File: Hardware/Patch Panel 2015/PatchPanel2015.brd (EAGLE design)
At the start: 226 x 119 mm, 35 parts

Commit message: Hi
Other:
- board size 226 x 119 mm -> 209.6 x 127 mm
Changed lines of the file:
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@@
 <?xml version="1.0" encoding="utf-8"?>
 <!DOCTYPE eagle SYSTEM "eagle.dtd">
-<eagle version="7.0.0">
+<eagle version="7.2.0">
 <drawing>
 <settings>
@@
 <board>
 <plain>
-<wire x1="0" y1="0" x2="226.04" y2="0" width="0" layer="20"/>
-<wire x1="226.04" y1="0" x2="226.04" y2="119.05" width="0" layer="20"/>
-<wire x1="226.04" y1="119.05" x2="0" y2="119.05" width="0" layer="20"/>
-<wire x1="0" y1="119.05" x2="0" y2="0" width="0" layer="20"/>
+<wire x1="0" y1="0" x2="209.55" y2="0" width="0" layer="20"/>
+<wire x1="209.55" y1="0" x2="209.55" y2="127" width="0" layer="20"/>
+<wire x1="209.55" y1="127" x2="0" y2="127" width="0" layer="20"/>
+<wire x1="0" y1="127" x2="0" y2="0" width="0" layer="20"/>
 <hole x="6.35" y="6.35" drill="5.5372"/>
 <hole x="50.8" y="6.35" drill="5.5372"/>

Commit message: hi eric, how are you?
also I made slight changes on the patch panel.
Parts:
- added EXT_MOTOR_1, EXT_MOTOR_2, EXT_MOTOR_3, EXT_MOTOR_4, EXT_MOTOR_5, EXT_MOTOR_6: XT60_BOARD_MOUNT, MRDT-2015-PowerBoard:XT60_BOARD
- added INT_MOTOR_1, INT_MOTOR_2, INT_MOTOR_3, INT_MOTOR_4, INT_MOTOR_5, INT_MOTOR_6: H_20020618-M02VERT, MRDT-2015-PowerBoard:20020620-M02
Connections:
- removed net VEE: ETH_IN7.4, ETH_IN7.5, ETH_OUT7.4, ETH_OUT7.5
- new net N$12: EXT_MOTOR_3.POS, INT_MOTOR_3.L1, INT_MOTOR_3.L2
- new net N$13: EXT_MOTOR_3.NEG, INT_MOTOR_3.R1, INT_MOTOR_3.R2
- new net N$15: EXT_MOTOR_4.POS, INT_MOTOR_4.L1, INT_MOTOR_4.L2
- new net N$16: EXT_MOTOR_4.NEG, INT_MOTOR_4.R1, INT_MOTOR_4.R2
- new net N$20: EXT_MOTOR_5.POS, INT_MOTOR_5.L1, INT_MOTOR_5.L2
- new net N$21: EXT_MOTOR_5.NEG, INT_MOTOR_5.R1, INT_MOTOR_5.R2
- new net N$23: EXT_MOTOR_6.POS, INT_MOTOR_6.L1, INT_MOTOR_6.L2
- new net N$24: EXT_MOTOR_6.NEG, INT_MOTOR_6.R1, INT_MOTOR_6.R2
- new net N$4: EXT_MOTOR_1.POS, INT_MOTOR_1.L1, INT_MOTOR_1.L2
- new net N$5: EXT_MOTOR_1.NEG, INT_MOTOR_1.R1, INT_MOTOR_1.R2
- new net N$7: EXT_MOTOR_2.POS, INT_MOTOR_2.L1, INT_MOTOR_2.L2
- new net N$8: EXT_MOTOR_2.NEG, INT_MOTOR_2.R1, INT_MOTOR_2.R2
- net +12V: now also ETH_IN7.4, ETH_IN7.5, ETH_OUT7.4, ETH_OUT7.5
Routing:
- net N$42: track 37.1 -> 0.00 mm
- net N$18: track 37.1 -> 0.00 mm
- net N$2: track 37.1 -> 0.00 mm
- net N$10: track 37.1 -> 0.00 mm
- net N$39: track 37.1 -> 0.00 mm
- net N$31: track 37.1 -> 0.00 mm
- net N$9: track 28.4 -> 0.00 mm
- net N$1: track 28.4 -> 0.00 mm
- net N$41: track 28.4 -> 0.00 mm
- net N$32: track 28.4 -> 0.00 mm
- net N$17: track 28.4 -> 0.00 mm
- net N$40: track 28.4 -> 0.00 mm
- net N$6: track 27.1 -> 0.00 mm
- net N$46: track 27.1 -> 0.00 mm
- net N$35: track 27.1 -> 0.00 mm
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
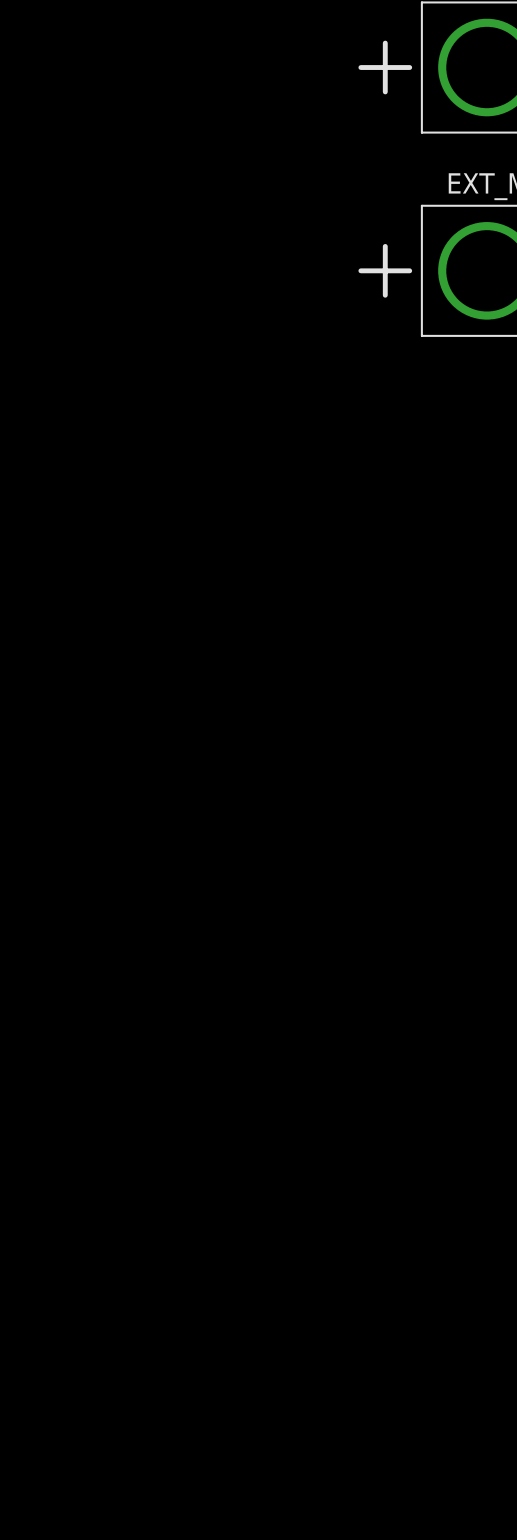
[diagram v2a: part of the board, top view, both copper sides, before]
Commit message: Eric, pls respond
Also, patch panel schematic is usable, but I haven’t started placement
or routing yet. I want to add PTCs to all of the PoRC outputs.
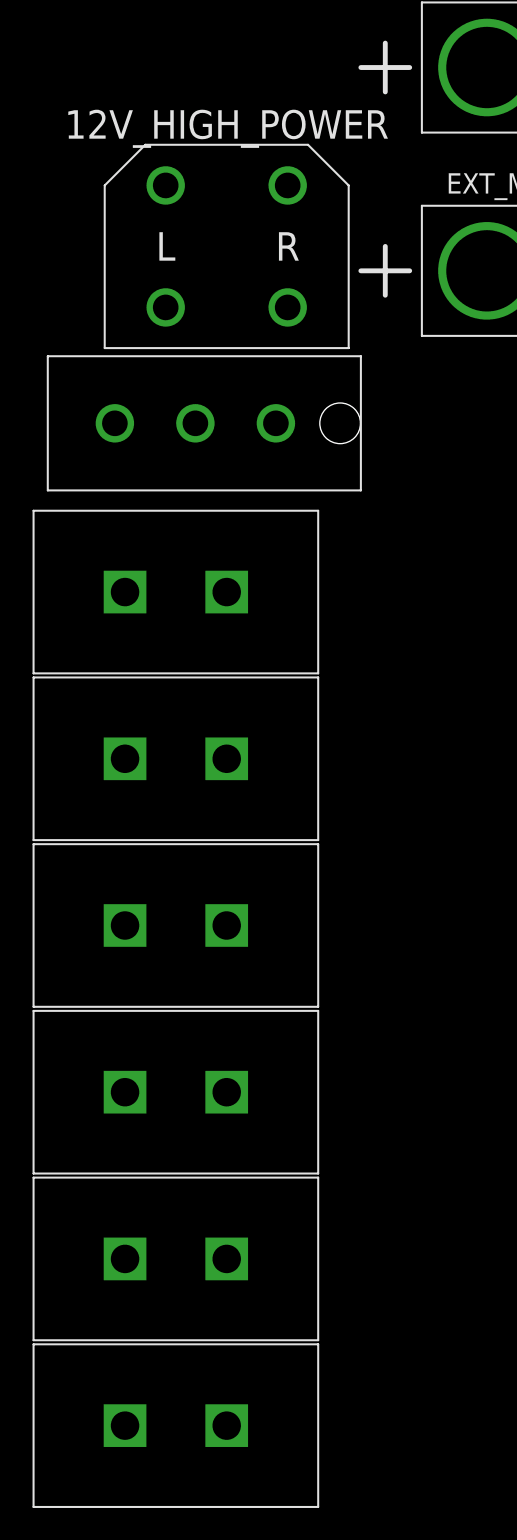
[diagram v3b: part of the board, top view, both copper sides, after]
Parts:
- added 12V_HIGH_POWER: H_20020618-M02VERT, MRDT-2015-PowerBoard:20020620-M02
- added U$1, U$2, U$3, U$5, U$6, U$8: MLX-2, MLX:42002-2
- added U$7: 3PIN, molex-power:0.93"
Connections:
- new net N$25: ARM_POWER.L, U$7.1
- new net V+: 12V_HIGH_POWER.L1, 12V_HIGH_POWER.L2, U$1.P$2, U$2.P$2, U$3.P$2, U$5.P$2, U$6.P$2, U$7.3, U$8.P$2
- net GND: now also 12V_HIGH_POWER.R1, 12V_HIGH_POWER.R2, ARM_POWER.R, U$1.P$1, U$2.P$1, U$3.P$1, U$5.P$1, U$6.P$1, U$7.2, U$8.P$1
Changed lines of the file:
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@@
 <element name="EXT_MOTOR_5" library="MRDT-2015-PowerBoard" package="XT60_BOARD" value="XT60_BOARD_MOUNT" x="-132.08" y="-408.94"/>
 <element name="EXT_MOTOR_6" library="MRDT-2015-PowerBoard" package="XT60_BOARD" value="XT60_BOARD_MOUNT" x="-132.08" y="-421.64"/>
+<element name="12V_HIGH_POWER" library="MRDT-2015-PowerBoard" package="20020620-M02" value="H_20020618-M02VERT" x="-144.272" y="-419.862">
+<attribute name="DIGIKEY_PN" value="609-3948-ND" x="-144.272" y="-419.862" size="1.778" layer="27" display="off"/>
+</element>
+<element name="U$7" library="molex-power" package="0.93&quot;" value="3PIN" x="-155.448" y="-431.292"/>
+<element name="U$8" library="MLX" package="42002-2" value="MLX-2" x="-150.622" y="-437.642"/>
+<element name="U$1" library="MLX" package="42002-2" value="MLX-2" x="-150.622" y="-448.056"/>
+<element name="U$2" library="MLX" package="42002-2" value="MLX-2" x="-150.622" y="-458.47"/>
+<element name="U$3" library="MLX" package="42002-2" value="MLX-2" x="-150.622" y="-468.884"/>
+<element name="U$5" library="MLX" package="42002-2" value="MLX-2" x="-150.622" y="-479.298"/>
+<element name="U$6" library="MLX" package="42002-2" value="MLX-2" x="-150.622" y="-489.712"/>
 </elements>
 <signals>
@@
 <contactref element="RS-485_OUT9" pad="8"/>
 <contactref element="RS-485_OUT9" pad="7"/>
-<wire x1="184.785" y1="6.775" x2="183.515" y2="4.235" width="0" layer="19" extent="1-16"/>
+<contactref element="U$7" pad="2"/>
+<contactref element="12V_HIGH_POWER" pad="R1"/>
+<contactref element="12V_HIGH_POWER" pad="R2"/>
+<contactref element="ARM_POWER" pad="R"/>
+<contactref element="U$8" pad="P$1"/>
+<contactref element="U$2" pad="P$1"/>
+<contactref element="U$3" pad="P$1"/>
+<contactref element="U$5" pad="P$1"/>
+<contactref element="U$6" pad="P$1"/>
+<contactref element="U$1" pad="P$1"/>
 <wire x1="-15.875" y1="-225.215" x2="-17.145" y2="-227.755" width="0" layer="19" extent="1-1"/>
 <wire x1="-17.145" y1="-209.975" x2="-15.875" y2="-225.215" width="0" layer="19" extent="1-1"/>
@@
 <wire x1="-17.145" y1="-334.435" x2="-15.875" y2="-331.895" width="0" layer="19" extent="1-1"/>
 <wire x1="-12.18" y1="-31.75" x2="-15.875" y2="-47.415" width="0" layer="19" extent="1-1"/>
+<wire x1="-21.07" y1="-31.75" x2="-12.18" y2="-31.75" width="0" layer="19" extent="1-1"/>
 <wire x1="-3.29" y1="-31.75" x2="-12.18" y2="-31.75" width="0" layer="19" extent="1-1"/>
 <wire x1="13.335" y1="-22.015" x2="-3.29" y2="-31.75" width="0" layer="19" extent="1-1"/>
@@
 <wire x1="184.785" y1="28.785" x2="183.515" y2="31.325" width="0" layer="19" extent="1-1"/>
 <wire x1="184.785" y1="6.775" x2="184.785" y2="28.785" width="0" layer="19" extent="1-1"/>
+<wire x1="183.515" y1="4.235" x2="184.785" y2="6.775" width="0" layer="19" extent="1-1"/>
+<wire x1="-140.462" y1="-412.242" x2="-17.145" y2="-334.435" width="0" layer="19" extent="1-1"/>
+<wire x1="-140.462" y1="-419.862" x2="-140.462" y2="-412.242" width="0" layer="19" extent="1-1"/>
+<wire x1="-146.2278" y1="-427.101" x2="-140.462" y2="-419.862" width="0" layer="19" extent="1-1"/>
+<wire x1="-150.622" y1="-437.642" x2="-146.2278" y2="-427.101" width="0" layer="19" extent="1-1"/>
+<wire x1="-150.622" y1="-448.056" x2="-150.622" y2="-437.642" width="0" layer="19" extent="1-1"/>
+<wire x1="-150.622" y1="-458.47" x2="-150.622" y2="-448.056" width="0" layer="19" extent="1-1"/>
+<wire x1="-150.622" y1="-468.884" x2="-150.622" y2="-458.47" width="0" layer="19" extent="1-1"/>
+<wire x1="-150.622" y1="-479.298" x2="-150.622" y2="-468.884" width="0" layer="19" extent="1-1"/>
+<wire x1="-150.622" y1="-489.712" x2="-150.622" y2="-479.298" width="0" layer="19" extent="1-1"/>
 </signal>
 <signal name="+12V">
@@
 <wire x1="-120.904" y1="-417.576" x2="-123.19" y2="-344.17" width="0" layer="19" extent="1-1"/>
 </signal>
+<signal name="N$25">
+<contactref element="ARM_POWER" pad="L"/>
+<contactref element="U$7" pad="1"/>
+<wire x1="-24.65" y1="-31.75" x2="-141.1986" y2="-427.101" width="0" layer="19" extent="1-1"/>
+</signal>
+<signal name="V+">
+<contactref element="U$7" pad="3"/>
+<contactref element="12V_HIGH_POWER" pad="L2"/>
+<contactref element="12V_HIGH_POWER" pad="L1"/>
+<contactref element="U$8" pad="P$2"/>
+<contactref element="U$1" pad="P$2"/>
+<contactref element="U$2" pad="P$2"/>
+<contactref element="U$3" pad="P$2"/>
+<contactref element="U$5" pad="P$2"/>
+<contactref element="U$6" pad="P$2"/>
+<wire x1="-144.272" y1="-479.298" x2="-144.272" y2="-489.712" width="0" layer="19" extent="1-1"/>
+<wire x1="-144.272" y1="-468.884" x2="-144.272" y2="-479.298" width="0" layer="19" extent="1-1"/>
+<wire x1="-144.272" y1="-458.47" x2="-144.272" y2="-468.884" width="0" layer="19" extent="1-1"/>
+<wire x1="-144.272" y1="-448.056" x2="-144.272" y2="-458.47" width="0" layer="19" extent="1-1"/>
+<wire x1="-144.272" y1="-437.642" x2="-144.272" y2="-448.056" width="0" layer="19" extent="1-1"/>
+<wire x1="-151.257" y1="-427.101" x2="-144.272" y2="-437.642" width="0" layer="19" extent="1-1"/>
+<wire x1="-148.082" y1="-419.862" x2="-151.257" y2="-427.101" width="0" layer="19" extent="1-1"/>
+<wire x1="-148.082" y1="-412.242" x2="-148.082" y2="-419.862" width="0" layer="19" extent="1-1"/>
+</signal>
 </signals>

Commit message: Patch Board layout
Attempt #1 of the layout of the Patch Board
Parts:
- moved EXT_MOTOR_6 613.8 mm to (192.5, 99.3)
- moved EXT_MOTOR_5 579.2 mm to (192.3, 70.9)
- moved INT_MOTOR_6 569.9 mm to (200.2, 122.4), flipped to the bottom, turned to 180 degrees
- moved U$8 563.5 mm to (38.4, 93.2), turned to 180 degrees
- moved U$1 563.3 mm to (38.4, 82.5), turned to 180 degrees
- moved U$2 563.0 mm to (38.4, 71.9), turned to 180 degrees
- moved U$3 562.8 mm to (38.4, 61.2), turned to 180 degrees
- moved U$5 562.8 mm to (38.4, 50.8), turned to 180 degrees
- moved U$6 562.8 mm to (38.4, 40.4), turned to 180 degrees
- moved 12V_HIGH_POWER 562.5 mm to (36.6, 112.8)
- moved U$7 560.6 mm to (26.2, 99.1)
- moved EXT_MOTOR_4 545.1 mm to (192.3, 41.9)
- moved INT_MOTOR_5 536.4 mm to (199.9, 94.2), flipped to the bottom, turned to 180 degrees
- moved INT_MOTOR_4 502.5 mm to (199.9, 65.3), flipped to the bottom, turned to 180 degrees
- moved RS-485_OUT17 462.0 mm to (60.5, 115.8), turned to 180 degrees
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
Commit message: Patch Board layout
layout design of the patch Board
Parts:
- moved U$7 75.3 mm to (37.3, 24.6)
- moved RS-485_OUT11 35.2 mm to (146.8, 98.6)
- moved RS-485_OUT8 34.5 mm to (146.8, 59.7)
- moved ETH_IN6 31.2 mm to (167.9, 9.65)
- moved ETH_OUT6 31.2 mm to (167.9, 22.4)
- moved RS-485_OUT2 24.8 mm to (78.2, 60.2)
- moved RS-485_OUT17 24.8 mm to (78.0, 98.3)
- moved ETH_IN5 24.1 mm to (147.8, 9.91)
- moved ETH_OUT5 24.1 mm to (147.8, 22.6)
- moved RS-485_OUT12 23.6 mm to (134.1, 116.6)
- moved RS-485_OUT13 22.7 mm to (123.4, 98.3)
- moved RS-485_OUT7 21.4 mm to (136.1, 42.2)
- moved RS-485_OUT6 20.9 mm to (124.0, 59.9)
- moved RS-485_OUT15 17.9 mm to (100.8, 98.3)
- moved RS-485_OUT4 17.0 mm to (100.8, 60.2)
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
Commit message: Patch Board Layout
Possibly final layout
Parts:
- moved RS-485_OUT3 79.7 mm to (113.0, 118.1), turned to 180 degrees
- moved RS-485_OUT5 79.2 mm to (134.6, 118.1), turned to 180 degrees
- moved RS-485_OUT7 78.6 mm to (156.2, 118.1), turned to 180 degrees
- moved RS-485_OUT16 77.8 mm to (91.4, 39.4), turned to 0 degrees
- moved RS-485_OUT14 77.2 mm to (113.0, 39.4), turned to 0 degrees
- moved RS-485_OUT12 77.2 mm to (134.6, 39.4), turned to 0 degrees
- moved 5V_EXT 77.1 mm to (74.9, 77.5)
- moved RS-485_OUT11 59.9 mm to (156.2, 39.4), turned to 0 degrees
- moved RS-485_OUT2 44.3 mm to (101.6, 97.8), turned to 180 degrees
- moved RS-485_OUT4 43.7 mm to (123.2, 97.8), turned to 180 degrees
- moved RS-485_OUT6 43.2 mm to (144.8, 97.8), turned to 180 degrees
- moved RS-485_OUT17 38.7 mm to (80.0, 59.7), turned to 0 degrees
- moved RS-485_OUT15 38.6 mm to (101.6, 59.7), turned to 0 degrees
- moved RS-485_OUT13 38.6 mm to (123.2, 59.7), turned to 0 degrees
- moved RS-485_OUT10 38.5 mm to (144.8, 59.7), turned to 0 degrees
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
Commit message: Added bound plane and approved layout.
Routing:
- added copper zone on layer 16, net GND
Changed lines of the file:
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@@
 <?xml version="1.0" encoding="utf-8"?>
 <!DOCTYPE eagle SYSTEM "eagle.dtd">
-<eagle version="6.5.0">
+<eagle version="6.6.0">
 <drawing>
 <settings>
@@
 <grid distance="0.05" unitdist="inch" unit="inch" style="lines" multiple="1" display="yes" altdistance="0.025" altunitdist="inch" altunit="inch"/>
 <layers>
-<layer number="1" name="Top" color="4" fill="1" visible="no" active="yes"/>
+<layer number="1" name="Top" color="4" fill="1" visible="yes" active="yes"/>
 <layer number="2" name="Route2" color="1" fill="3" visible="no" active="no"/>
 <layer number="3" name="Route3" color="4" fill="3" visible="no" active="no"/>
@@
 <contactref element="U$6" pad="P$1"/>
 <contactref element="U$1" pad="P$1"/>
-<wire x1="161.925" y1="84.245" x2="163.195" y2="86.785" width="0" layer="19" extent="1-1"/>
-<wire x1="170.815" y1="71.965" x2="161.925" y2="84.245" width="0" layer="19" extent="1-1"/>
-<wire x1="169.545" y1="69.425" x2="170.815" y2="71.965" width="0" layer="19" extent="1-1"/>
-<wire x1="149.225" y1="66.885" x2="169.545" y2="69.425" width="0" layer="19" extent="1-1"/>
-<wire x1="147.955" y1="64.345" x2="149.225" y2="66.885" width="0" layer="19" extent="1-1"/>
-<wire x1="139.065" y1="46.565" x2="147.955" y2="64.345" width="0" layer="19" extent="1-1"/>
-<wire x1="137.795" y1="44.025" x2="139.065" y2="46.565" width="0" layer="19" extent="1-1"/>
-<wire x1="139.065" y1="28.785" x2="137.795" y2="44.025" width="0" layer="19" extent="1-1"/>
-<wire x1="140.335" y1="26.245" x2="139.065" y2="28.785" width="0" layer="19" extent="1-1"/>
-<wire x1="159.385" y1="44.025" x2="139.065" y2="46.565" width="0" layer="19" extent="1-1"/>
-<wire x1="160.655" y1="46.565" x2="159.385" y2="44.025" width="0" layer="19" extent="1-1"/>
-<wire x1="160.655" y1="28.785" x2="159.385" y2="44.025" width="0" layer="19" extent="1-1"/>
-<wire x1="161.925" y1="26.245" x2="160.655" y2="28.785" width="0" layer="19" extent="1-1"/>
-<wire x1="182.245" y1="28.785" x2="161.925" y2="26.245" width="0" layer="19" extent="1-1"/>
-<wire x1="183.515" y1="26.245" x2="182.245" y2="28.785" width="0" layer="19" extent="1-1"/>
-<wire x1="127.635" y1="66.885" x2="147.955" y2="64.345" width="0" layer="19" extent="1-1"/>
-<wire x1="126.365" y1="64.345" x2="127.635" y2="66.885" width="0" layer="19" extent="1-1"/>
-<wire x1="117.475" y1="46.565" x2="126.365" y2="64.345" width="0" layer="19" extent="1-1"/>
-<wire x1="116.205" y1="44.025" x2="117.475" y2="46.565" width="0" layer="19" extent="1-1"/>
-<wire x1="117.475" y1="28.785" x2="116.205" y2="44.025" width="0" layer="19" extent="1-1"/>
-<wire x1="118.745" y1="26.245" x2="117.475" y2="28.785" width="0" layer="19" extent="1-1"/>
-<wire x1="106.045" y1="66.885" x2="126.365" y2="64.345" width="0" layer="19" extent="1-1"/>
-<wire x1="104.775" y1="64.345" x2="106.045" y2="66.885" width="0" layer="19" extent="1-1"/>
-<wire x1="95.885" y1="46.565" x2="104.775" y2="64.345" width="0" layer="19" extent="1-1"/>
-<wire x1="94.615" y1="44.025" x2="95.885" y2="46.565" width="0" layer="19" extent="1-1"/>
-<wire x1="95.885" y1="28.785" x2="94.615" y2="44.025" width="0" layer="19" extent="1-1"/>
-<wire x1="97.155" y1="26.245" x2="95.885" y2="28.785" width="0" layer="19" extent="1-1"/>
-<wire x1="84.455" y1="66.885" x2="104.775" y2="64.345" width="0" layer="19" extent="1-1"/>
-<wire x1="83.185" y1="64.345" x2="84.455" y2="66.885" width="0" layer="19" extent="1-1"/>
-<wire x1="73.14" y1="77.47" x2="84.455" y2="66.885" width="0" layer="19" extent="1-1"/>
-<wire x1="75.565" y1="90.595" x2="73.14" y2="77.47" width="0" layer="19" extent="1-1"/>
-<wire x1="76.835" y1="93.135" x2="75.565" y2="90.595" width="0" layer="19" extent="1-1"/>
-<wire x1="97.155" y1="90.595" x2="76.835" y2="93.135" width="0" layer="19" extent="1-1"/>
-<wire x1="98.425" y1="93.135" x2="97.155" y2="90.595" width="0" layer="19" extent="1-1"/>
-<wire x1="108.585" y1="110.915" x2="98.425" y2="93.135" width="0" layer="19" extent="1-1"/>
-<wire x1="109.855" y1="113.455" x2="108.585" y2="110.915" width="0" layer="19" extent="1-1"/>
-<wire x1="130.175" y1="110.915" x2="109.855" y2="113.455" width="0" layer="19" extent="1-1"/>
-<wire x1="131.445" y1="113.455" x2="130.175" y2="110.915" width="0" layer="19" extent="1-1"/>
-<wire x1="120.015" y1="93.135" x2="130.175" y2="110.915" width="0" layer="19" extent="1-1"/>
-<wire x1="118.745" y1="90.595" x2="120.015" y2="93.135" width="0" layer="19" extent="1-1"/>
-<wire x1="140.335" y1="90.595" x2="120.015" y2="93.135" width="0" layer="19" extent="1-1"/>
-<wire x1="141.605" y1="93.135" x2="140.335" y2="90.595" width="0" layer="19" extent="1-1"/>
-<wire x1="75.565" y1="26.245" x2="95.885" y2="28.785" width="0" layer="19" extent="1-1"/>
-<wire x1="74.295" y1="28.785" x2="75.565" y2="26.245" width="0" layer="19" extent="1-1"/>
-<wire x1="151.765" y1="110.915" x2="131.445" y2="113.455" width="0" layer="19" extent="1-1"/>
-<wire x1="153.035" y1="113.455" x2="151.765" y2="110.915" width="0" layer="19" extent="1-1"/>
-<wire x1="53.34" y1="71.12" x2="73.14" y2="77.47" width="0" layer="19" extent="1-1"/>
-<wire x1="53.34" y1="87.63" x2="53.34" y2="71.12" width="0" layer="19" extent="1-1"/>
-<wire x1="53.34" y1="104.14" x2="53.34" y2="87.63" width="0" layer="19" extent="1-1"/>
-<wire x1="53.34" y1="120.65" x2="53.34" y2="104.14" width="0" layer="19" extent="1-1"/>
-<wire x1="53.34" y1="54.61" x2="53.34" y2="71.12" width="0" layer="19" extent="1-1"/>
-<wire x1="53.34" y1="38.1" x2="53.34" y2="54.61" width="0" layer="19" extent="1-1"/>
-<wire x1="49.8602" y1="20.701" x2="53.34" y2="38.1" width="0" layer="19" extent="1-1"/>
-<wire x1="55.36" y1="3.81" x2="49.8602" y2="20.701" width="0" layer="19" extent="1-1"/>
-<wire x1="41.39" y1="3.81" x2="55.36" y2="3.81" width="0" layer="19" extent="1-1"/>
-<wire x1="74.295" y1="1.695" x2="55.36" y2="3.81" width="0" layer="19" extent="1-1"/>
-<wire x1="75.565" y1="4.235" x2="74.295" y2="1.695" width="0" layer="19" extent="1-1"/>
-<wire x1="95.885" y1="1.695" x2="75.565" y2="4.235" width="0" layer="19" extent="1-1"/>
-<wire x1="97.155" y1="4.235" x2="95.885" y2="1.695" width="0" layer="19" extent="1-1"/>
-<wire x1="117.475" y1="1.695" x2="97.155" y2="4.235" width="0" layer="19" extent="1-1"/>
-<wire x1="118.745" y1="4.235" x2="117.475" y2="1.695" width="0" layer="19" extent="1-1"/>
-<wire x1="139.065" y1="1.695" x2="118.745" y2="4.235" width="0" layer="19" extent="1-1"/>
-<wire x1="140.335" y1="4.235" x2="139.065" y2="1.695" width="0" layer="19" extent="1-1"/>
-<wire x1="160.655" y1="1.695" x2="140.335" y2="4.235" width="0" layer="19" extent="1-1"/>
-<wire x1="161.925" y1="4.235" x2="160.655" y2="1.695" width="0" layer="19" extent="1-1"/>
-<wire x1="182.245" y1="1.695" x2="161.925" y2="4.235" width="0" layer="19" extent="1-1"/>
-<wire x1="183.515" y1="4.235" x2="182.245" y2="1.695" width="0" layer="19" extent="1-1"/>
-<wire x1="19.685" y1="4.235" x2="41.39" y2="3.81" width="0" layer="19" extent="1-1"/>
-<wire x1="18.415" y1="1.695" x2="19.685" y2="4.235" width="0" layer="19" extent="1-1"/>
-<wire x1="19.685" y1="26.245" x2="19.685" y2="4.235" width="0" layer="19" extent="1-1"/>
-<wire x1="18.415" y1="28.785" x2="19.685" y2="26.245" width="0" layer="19" extent="1-1"/>
-<wire x1="86.36" y1="115.57" x2="108.585" y2="110.915" width="0" layer="19" extent="1-1"/>
-<wire x1="86.36" y1="123.19" x2="86.36" y2="115.57" width="0" layer="19" extent="1-1"/>
+<polygon width="0.4064" layer="16" thermals="no">
+<vertex x="-26.67" y="138.43"/>
+<vertex x="219.71" y="138.43"/>
+<vertex x="219.71" y="-6.35"/>
+<vertex x="-26.67" y="-6.35"/>
+</polygon>
 </signal>
 <signal name="+12V">
